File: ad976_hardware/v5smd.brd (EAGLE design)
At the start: 94.3 x 61.6 mm, 41 parts, among them IC1 317EMP, IC2 317EMP, IC3 337IMP, IC4 LM741P, IC5 LM741P

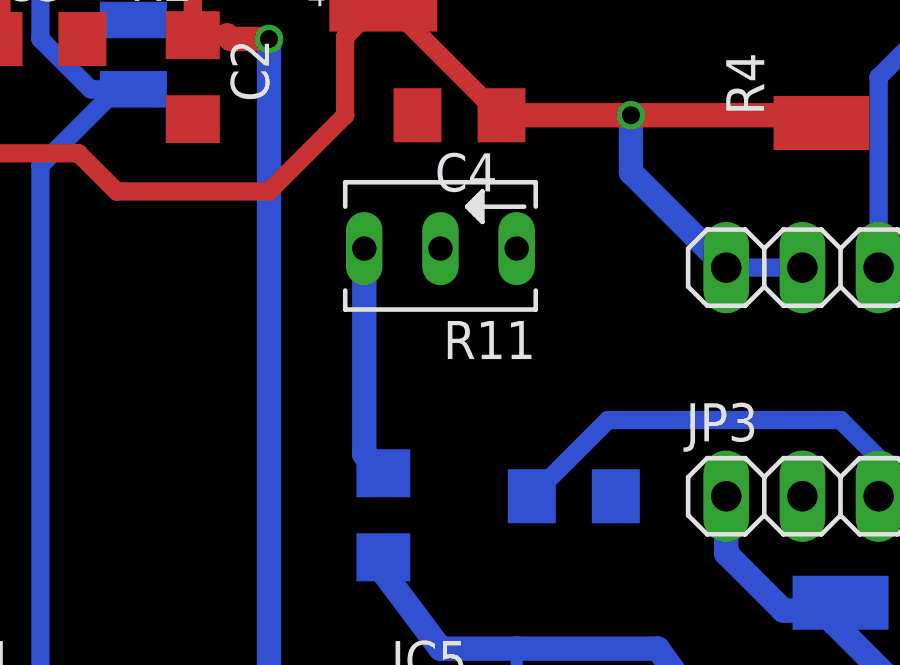
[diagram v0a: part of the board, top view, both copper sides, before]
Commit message: update
updated eagle schematic and pcam layout
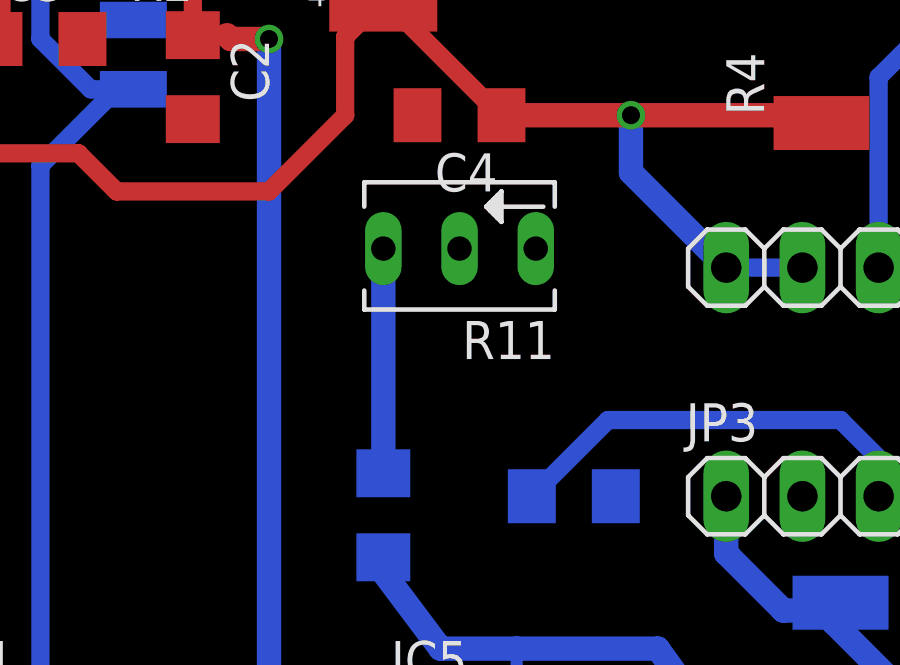
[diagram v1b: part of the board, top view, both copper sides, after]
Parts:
- moved R11 0.63 mm to (41.3, 41.3)
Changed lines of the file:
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@@
 <element name="R1" library="rcl" package="R2512" value="1.69k" x="29.845" y="57.15" rot="R180"/>
 <element name="R10" library="rcl" package="R2512" value="33k" x="34.29" y="15.24" rot="MR270"/>
-<element name="R11" library="pot" package="B64Y" value="5k" x="40.64" y="41.275" rot="R180"/>
+<element name="R11" library="pot" package="B64Y" value="5k" x="41.275" y="41.275" rot="R180"/>
 <element name="R12" library="rcl" package="R2512" value="33k" x="49.53" y="22.86" rot="MR90"/>
 <element name="R13" library="rcl" package="R2512" value="220" x="53.975" y="26.67" rot="MR270"/>
@@
 <contactref element="R11" pad="A"/>
 <contactref element="C9" pad="2"/>
-<wire x1="38.1" y1="41.275" x2="38.1" y2="34.42" width="0.8128" layer="16"/>
-<wire x1="38.1" y1="34.42" x2="38.735" y2="33.785" width="0.8128" layer="16"/>
+<wire x1="38.735" y1="41.275" x2="38.735" y2="33.785" width="0.8128" layer="16"/>
 </signal>
 <signal name="N$15">
